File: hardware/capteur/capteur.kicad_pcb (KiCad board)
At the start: 2 copper layers, 125 x 65 mm, 47 parts, among them J1 Pluvio, J10 RJ45, J11 Term_sel, J12 Conn_01x05_Male, J2 Conn_01x02_Male, J3 NMEA0183 (wind), J4 Conn_01x02_Male, J5 Conn_01x02_Male, J6 Conn_01x02_Male, J7 Conn_01x03_Male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

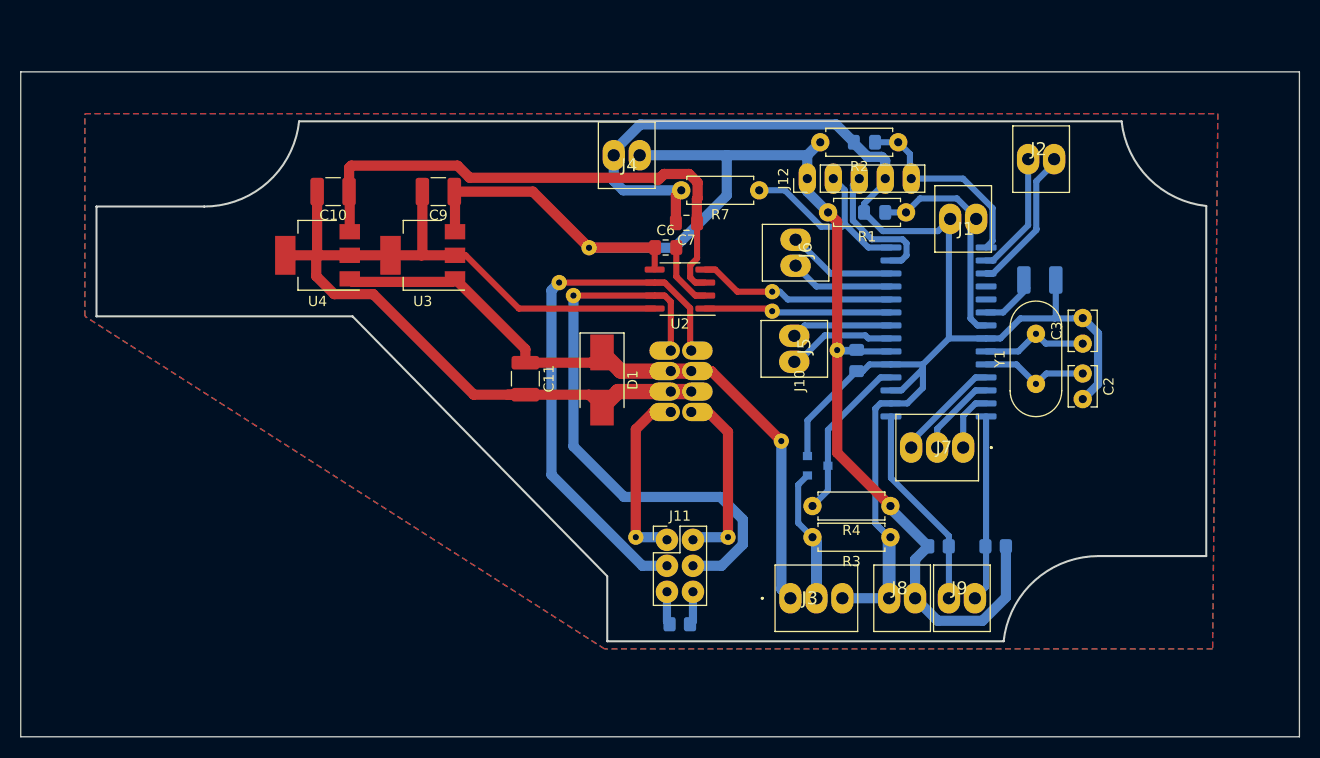
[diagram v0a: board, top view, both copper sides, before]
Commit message: Increase isolation to 0,3mm reroute PCB after schematic changes.
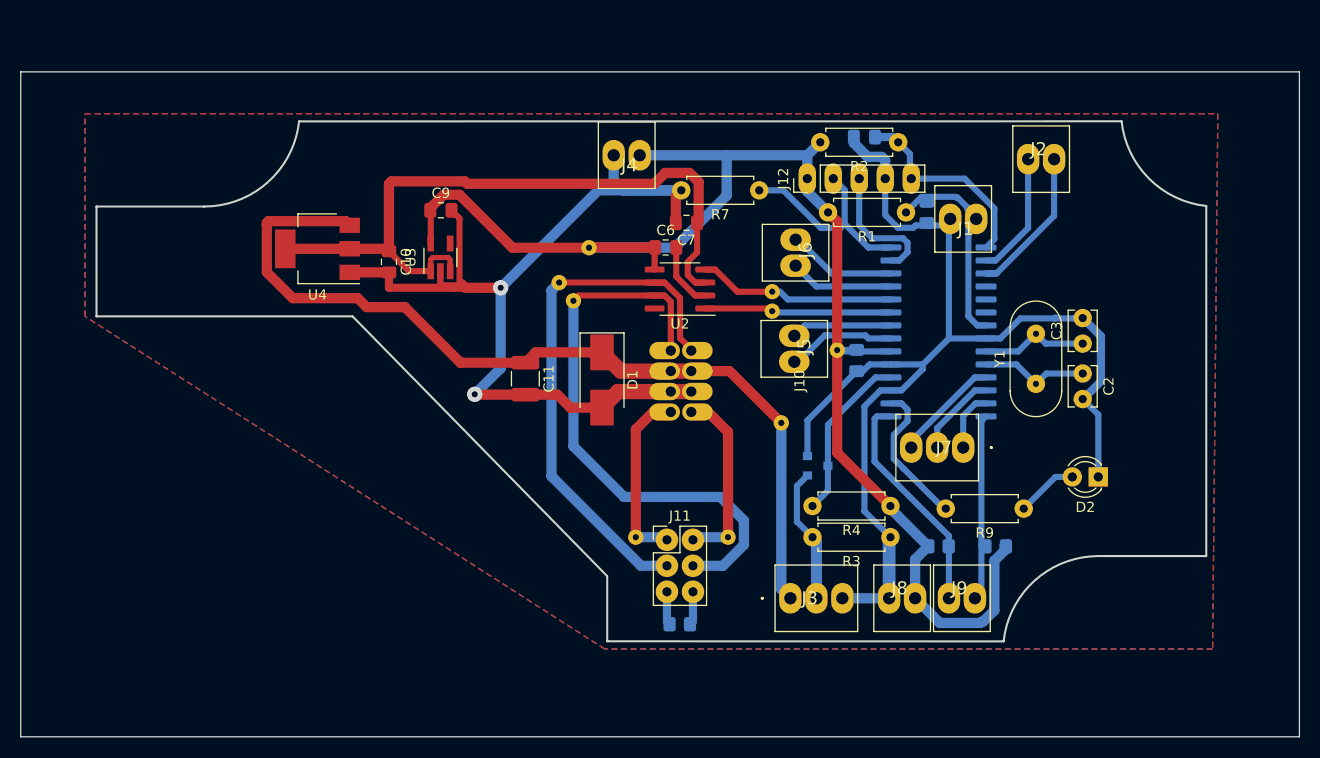
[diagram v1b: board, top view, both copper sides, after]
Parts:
- removed C5: 10uF, Capacitor_SMD:C_1210_3225Metric_Pad1.33x2.70mm_HandSolder
- added D2: RED, LED_THT:LED_D3.0mm, F.Cu at (180.3, 104.6)
- added R9: 330, Resistor_THT:R_Axial_DIN0207_L6.3mm_D2.5mm_P7.62mm_Horizontal, F.Cu at (173.1, 107.7)
- C10, C9: value 10uF -> 1uF; footprint Capacitor_SMD:C_1210_3225Metric_Pad1.33x2.70mm_HandSolder -> Capacitor_SMD:C_0805_2012Metric_Pad1.18x1.45mm_HandSolder
- U1: value PIC18F26K80_ISS -> PIC18F27Q84_ISS
- U2: value MCP2542FDxMF -> TLE9250VSJXUMA1
- U3: value uA7833 -> mic5504-3.3; footprint Package_TO_SOT_SMD:SOT-223-3_TabPin2 -> Package_TO_SOT_SMD:SOT-23-5_HandSoldering
- U4: value uA7805 -> LDL1117S50
- moved C10 8.77 mm to (111.0, 83.6), turned to 270 degrees
- moved C1 5.10 mm to (163.6, 78.7), turned to 90 degrees
- moved C9 1.85 mm to (116.1, 78.5), turned to 0 degrees
- moved ? 1.78 mm to (149.4, 99.3)
- moved U3 1.74 mm to (116.0, 83.1), turned to 90 degrees
- moved U4 0.63 mm to (104.0, 82.3)
- moved ? 0.51 mm to (129.0, 87.4)
- moved C8 0.51 mm to (157.5, 71.4)
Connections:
- U1 pad 16: GND -> Net-(R9-Pad2)
- U1 pad 4: Net-(U1-Pad4) -> GND
- U1 pad 5: Net-(U1-Pad5) -> GND
- U1 pad 6: Net-(C5-Pad2) -> GND
- U3 pad 1: +12V -> +5V
- U3 pad 3: +3V3 -> +5V
- U4 pad 1: +12V -> GND
- U4 pad 2: GND -> +5V
- U4 pad 3: +5V -> +12V
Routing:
- net GND: track 267.2 -> 224.2 mm, vias 0 -> 2
- net +12V: track 66.4 -> 87.9 mm
- net +5V: track 53.6 -> 68.9 mm
- net Net-(R9-Pad2): track 0.00 -> 14.3 mm
- net Net-(D2-Pad2): track 0.00 -> 6.03 mm
- net Net-(C5-Pad2): track 5.03 -> 0.00 mm
- net +3V3: track 137.4 -> 140.2 mm
- net /SDA: track 20.1 -> 22.3 mm
- net Net-(C1-Pad2): track 22.1 -> 20.5 mm
- net /PGC: track 13.4 -> 12.9 mm
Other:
- net class Default: clearance 0.2 -> 0.3
- rule trace_clearance: 0.2 -> 0.3

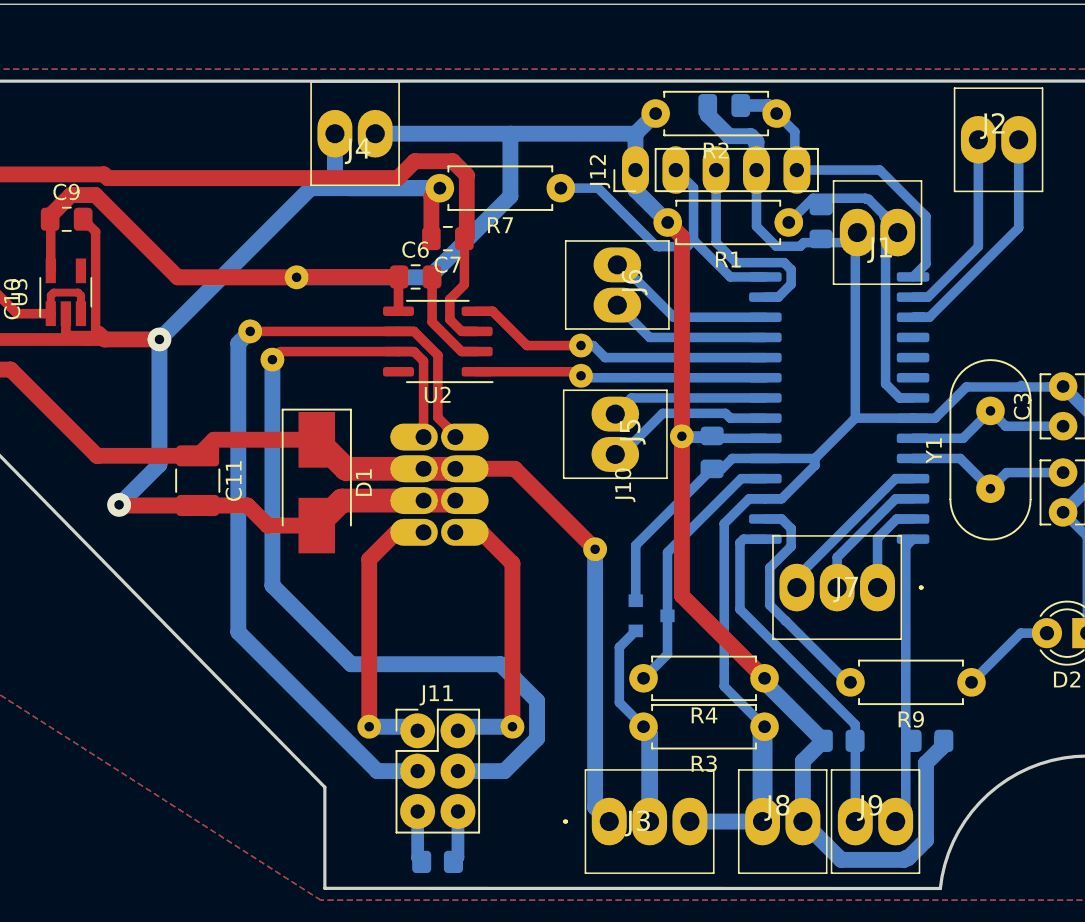
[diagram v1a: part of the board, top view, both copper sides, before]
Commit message: Enlarge some through-hole pad, for easier soldering
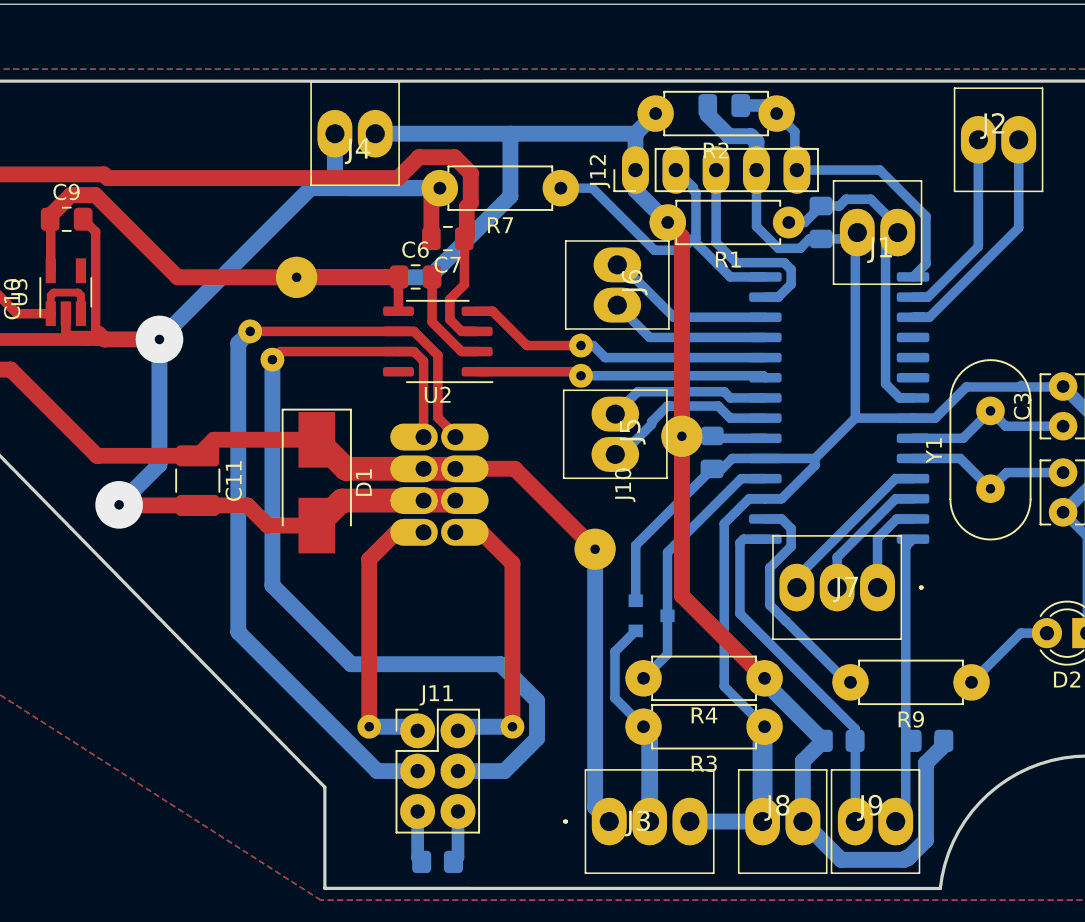
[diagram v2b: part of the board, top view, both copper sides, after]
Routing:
- net GND: track 224.2 -> 225.3 mm
- net +5V: track 68.9 -> 69.5 mm

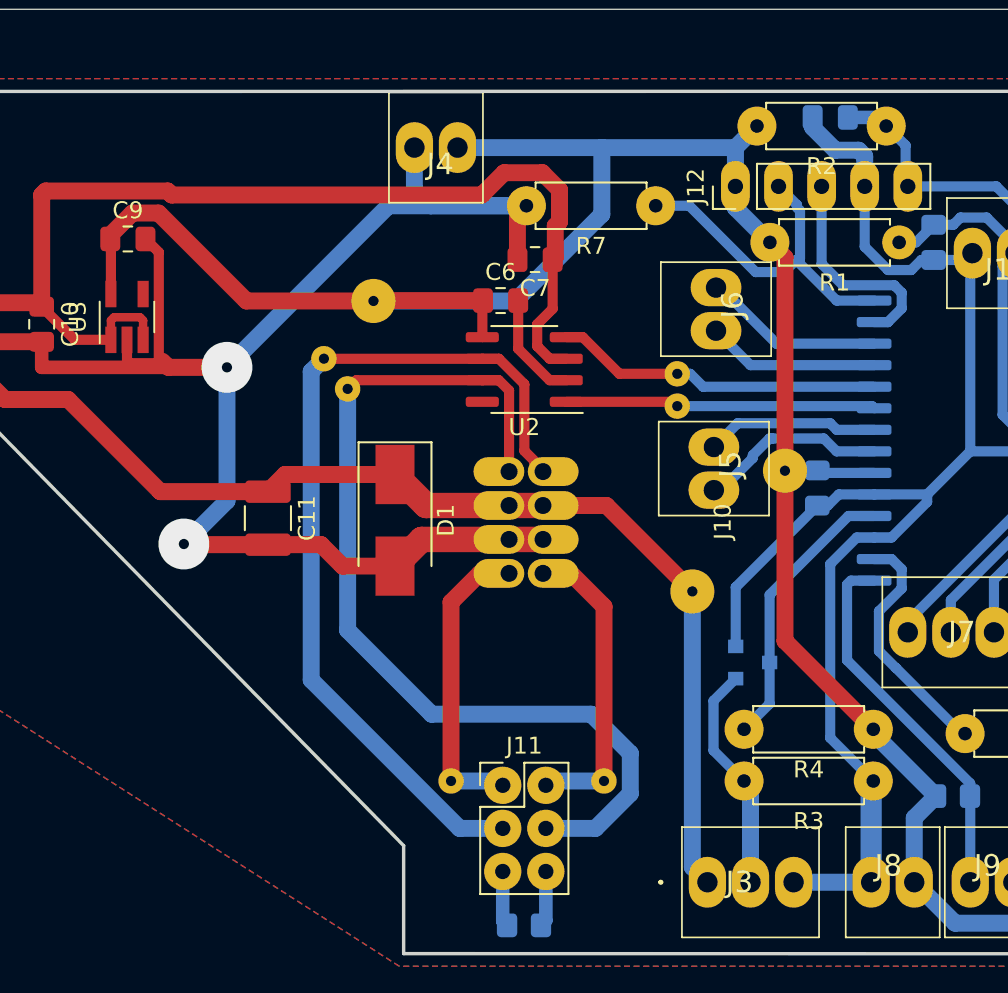
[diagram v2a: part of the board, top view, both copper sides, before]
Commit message: Convert back more pads to via. Move vias outside of component footprint
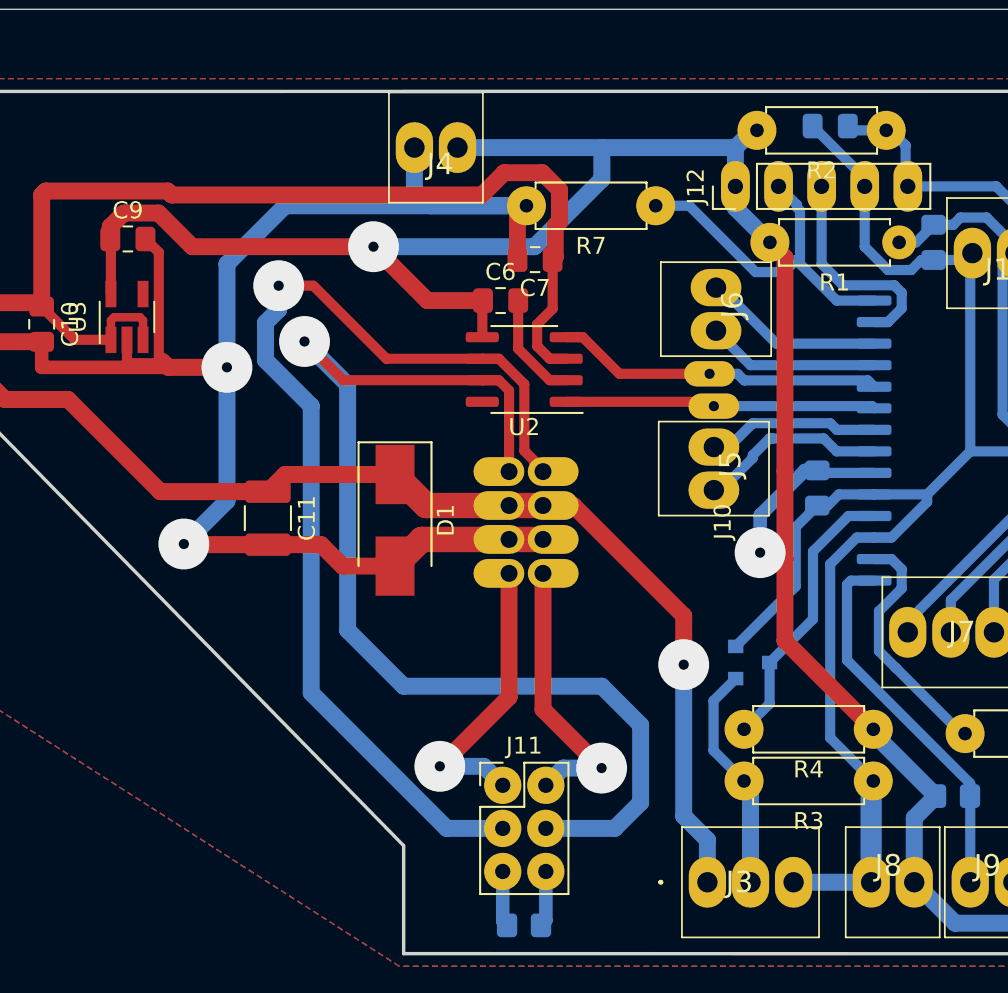
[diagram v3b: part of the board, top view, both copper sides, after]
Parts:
- removed the ? at (127.6, 85.6)
- removed the ? at (130.6, 82.2)
- removed the ? at (149.4, 99.3)
- removed the ? at (144.1, 110.5)
- removed the ? at (135.1, 110.5)
- removed the ? at (148.5, 88.4)
- removed the ? at (154.8, 92.2)
- removed the ? at (129.0, 87.4)
- added ?: , local:via_soldered, F.Cu at (150.6, 88.4)
- moved ? 1.91 mm to (150.4, 86.5)
- moved C8 0.51 mm to (157.5, 71.9)
- moved R2 0.25 mm to (160.8, 72.1)
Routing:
- net /CANL: track 52.2 -> 62.5 mm, vias 0 -> 1
- net /CANH: track 56.9 -> 66.5 mm, vias 0 -> 1
- net GND: track 225.3 -> 228.0 mm
- net +3V3: track 140.2 -> 142.4 mm, vias 0 -> 2
- net Net-(J10-Pad8): track 18.2 -> 16.6 mm, vias 0 -> 1
- net +12V: track 87.9 -> 86.8 mm, vias 0 -> 1
- net Net-(J10-Pad7): track 17.6 -> 17.2 mm, vias 0 -> 1

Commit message: Generate gerber files for new capteur version
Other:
- board size 125 x 65 mm -> 125 x 70 mm

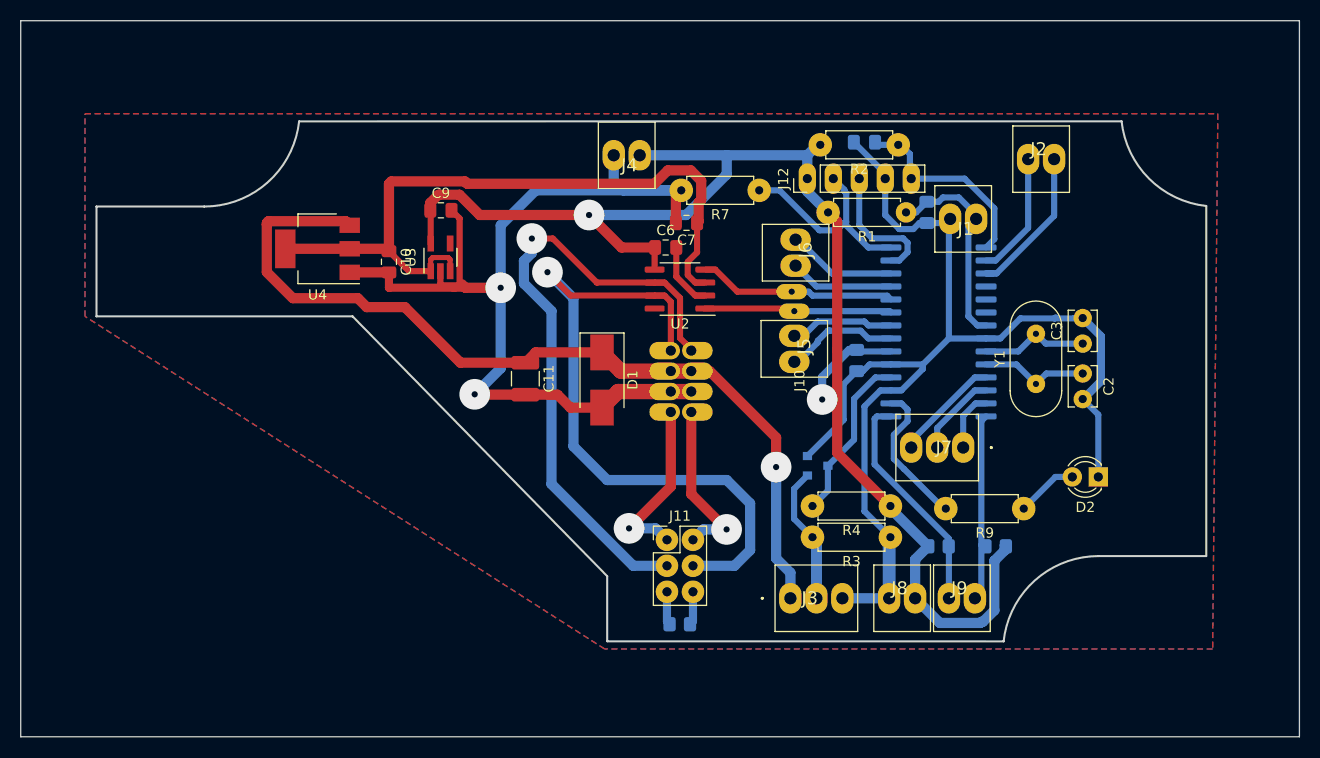
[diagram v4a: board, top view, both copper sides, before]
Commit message: update capteur & centrale to new kicad format
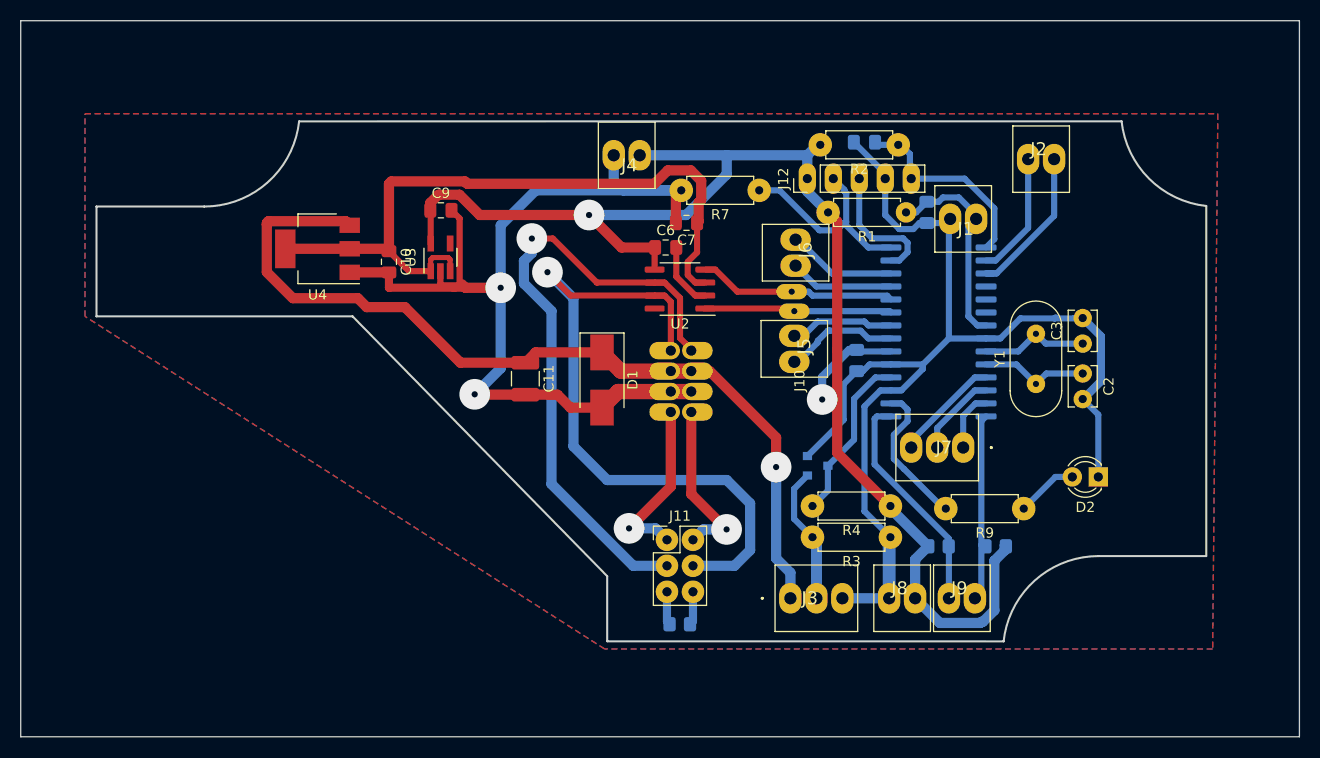
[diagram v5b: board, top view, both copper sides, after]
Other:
- net class Default removed
